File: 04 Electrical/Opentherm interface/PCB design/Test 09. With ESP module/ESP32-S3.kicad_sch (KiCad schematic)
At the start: 5 parts, among them U1 ESP32-S3-WROOM-1-N8R2

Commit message: Schematic update
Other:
- moved on the sheet: C1, C2, C3, R1, U1

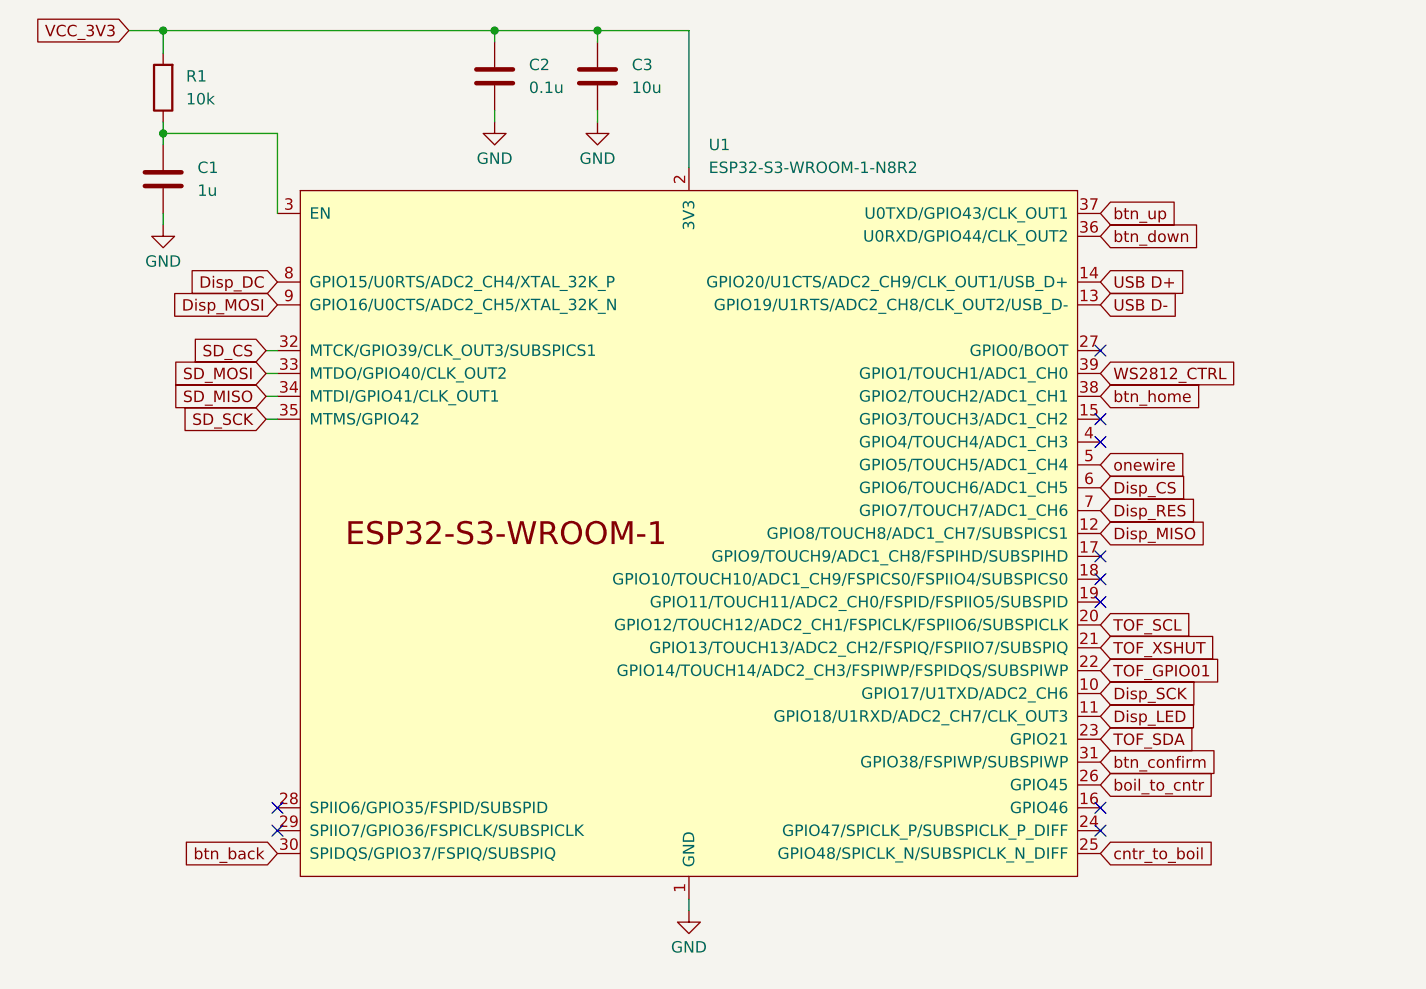
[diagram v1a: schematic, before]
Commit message: SPI port on default pins
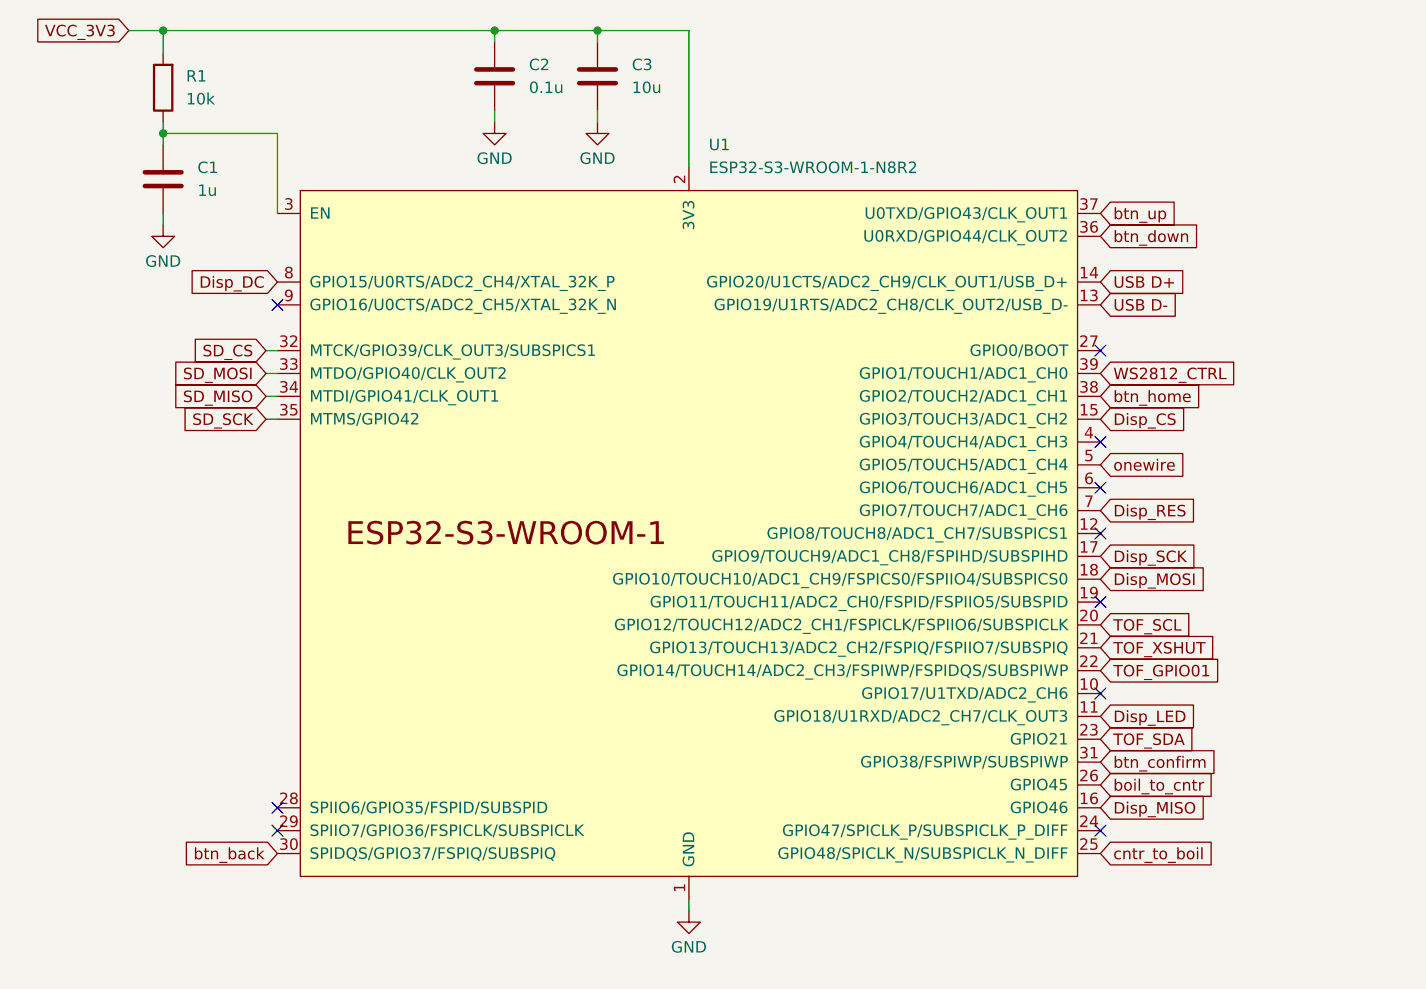
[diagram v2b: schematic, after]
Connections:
- net Disp_CS: now also U1.15 (GPIO3/TOUCH3/ADC1_CH2); no longer U1.6 (GPIO6/TOUCH6/ADC1_CH5)
- net Disp_MISO: now also U1.16 (GPIO46); no longer U1.12 (GPIO8/TOUCH8/ADC1_CH7/SUBSPICS1)
- net Disp_MOSI: now also U1.18 (GPIO10/TOUCH10/ADC1_CH9/FSPICS0/FSPIIO4/SUBSPICS0); no longer U1.9 (GPIO16/U0CTS/ADC2_CH5/XTAL_32K_N)
- net Disp_SCK: now also U1.17 (GPIO9/TOUCH9/ADC1_CH8/FSPIHD/SUBSPIHD); no longer U1.10 (GPIO17/U1TXD/ADC2_CH6)

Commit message: Component assignment
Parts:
- R1: footprint Resistor_SMD:R_0201_0603Metric -> Resistor_SMD:R_0603_1608Metric
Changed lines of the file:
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@@
 			)
 		)
-		(property "Footprint" "Resistor_SMD:R_0201_0603Metric"
+		(property "Footprint" "Resistor_SMD:R_0603_1608Metric"
 			(at 94.488 46.99 90)
 			(effects
